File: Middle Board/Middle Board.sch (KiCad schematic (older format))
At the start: 40 parts, among them J1 JTAG Connector, SW1 SW_SPST, U1 ATSAMG55, U2 BNO055_Breakout, U3 MS5803, U4 XBee_PRO_SX

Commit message: Added GPS to mainboard schematic
Went with a different GPS module than the one Daniel picked out since
we're going with external antennas
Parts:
- added D1, D2: LED_R, symbol LED
- added D3: LED_G, symbol LED
- added D4: LED_B, symbol LED
- added J? (x2): Conn_Coaxial, symbol Conn_Coaxial
- added R1, R2, R3, R4: 270, symbol R
- added R?: 100, symbol R
- added U?: PD0922J5050S2HF, symbol PD0922J5050S2HF
- gave numbers to parts that had none: 4
- renumbered D1 to D5, D2 to D6, D3 to D7, R6 to R10, R7 to R11, R8 to R12, R9 to R14, R10 to R15, R11 to R16, R1 to R5, R2 to R6, R3 to R7, R4 to R8, R5 to R9, U4 to U5
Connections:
- net +3V3: now also D1.2 (A), D2.2 (A), D3.2 (A), D4.2 (A)
- net GND: now also J?.2 (Ext), J?.2 (Ext), R1.2
- net at U1.6 (PA0): now also R2.2
- net at U1.61 (PA2): now also R4.2
- net at U1.7 (PA1): now also R3.2
- net XBEE_RF_50Ω: now reaches U4.2, U5.36 (RF_PAD)
- net ANT1_RF_50Ω: now reaches J2.1 (In), R13.1, U4.6
- net ANT2_RF_50Ω: now reaches J3.1 (In), R13.2, U4.4
- new net: D1.1 (K), R1.1
- new net: D2.1 (K), R2.1
- new net: D3.1 (K), R3.1
- new net: D4.1 (K), R4.1
- new net ANT3_RF_50Ω: J?.1 (In), R?.1, U?.6
- new net ANT4_RF_50Ω: J?.1 (In), R?.2, U?.4
- new net GPS_RF_50Ω: U?.2
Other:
- note added: "Might need more antenna connectors, 2 might not be enough\n"
- moved on the sheet: C1, C10, C11, C12, C13, C14, C15, C16, C2, C3, C4, C5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

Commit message: Apparently I forgot to save everything earlier
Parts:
- added BT1: CR_1220, symbol Battery_Cell
- added FL1: B39162B3520U410, symbol B39162B3520U410
- added R18, R19: 20, symbol R
- added U7: UBX_NEO_M8Q, symbol UBX_NEO_M8Q
- gave numbers to parts that had none: 4
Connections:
- net +3V3: now also U7.23 (VCC)
- net GND: now also BT1.2 (-), FL1.1 (GND), FL1.3 (GND), FL1.4 (GND), FL1.6 (GND), U7.10 (GND), U7.12 (GND), U7.13 (GND), U7.24 (GND), U7.7 (VDD_USB)
- net GPS_RF_50Ω: now also FL1.5 (OUT), U7.11 (RF_IN); no longer U6.2
- new net: R18.1, U7.20 (TxD)
- new net: R19.1, U7.21 (RxD)
- new net: BT1.1 (+), U7.22 (V_BCKP)
- new net GPS_FILT_RF_50Ω: FL1.2 (IN), U6.2
- new net GPS_RX: R19.2
- new net GPS_TX: R18.2
- no-connect marks 24 -> 34
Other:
- moved on the sheet: J4, J5, R17, U6

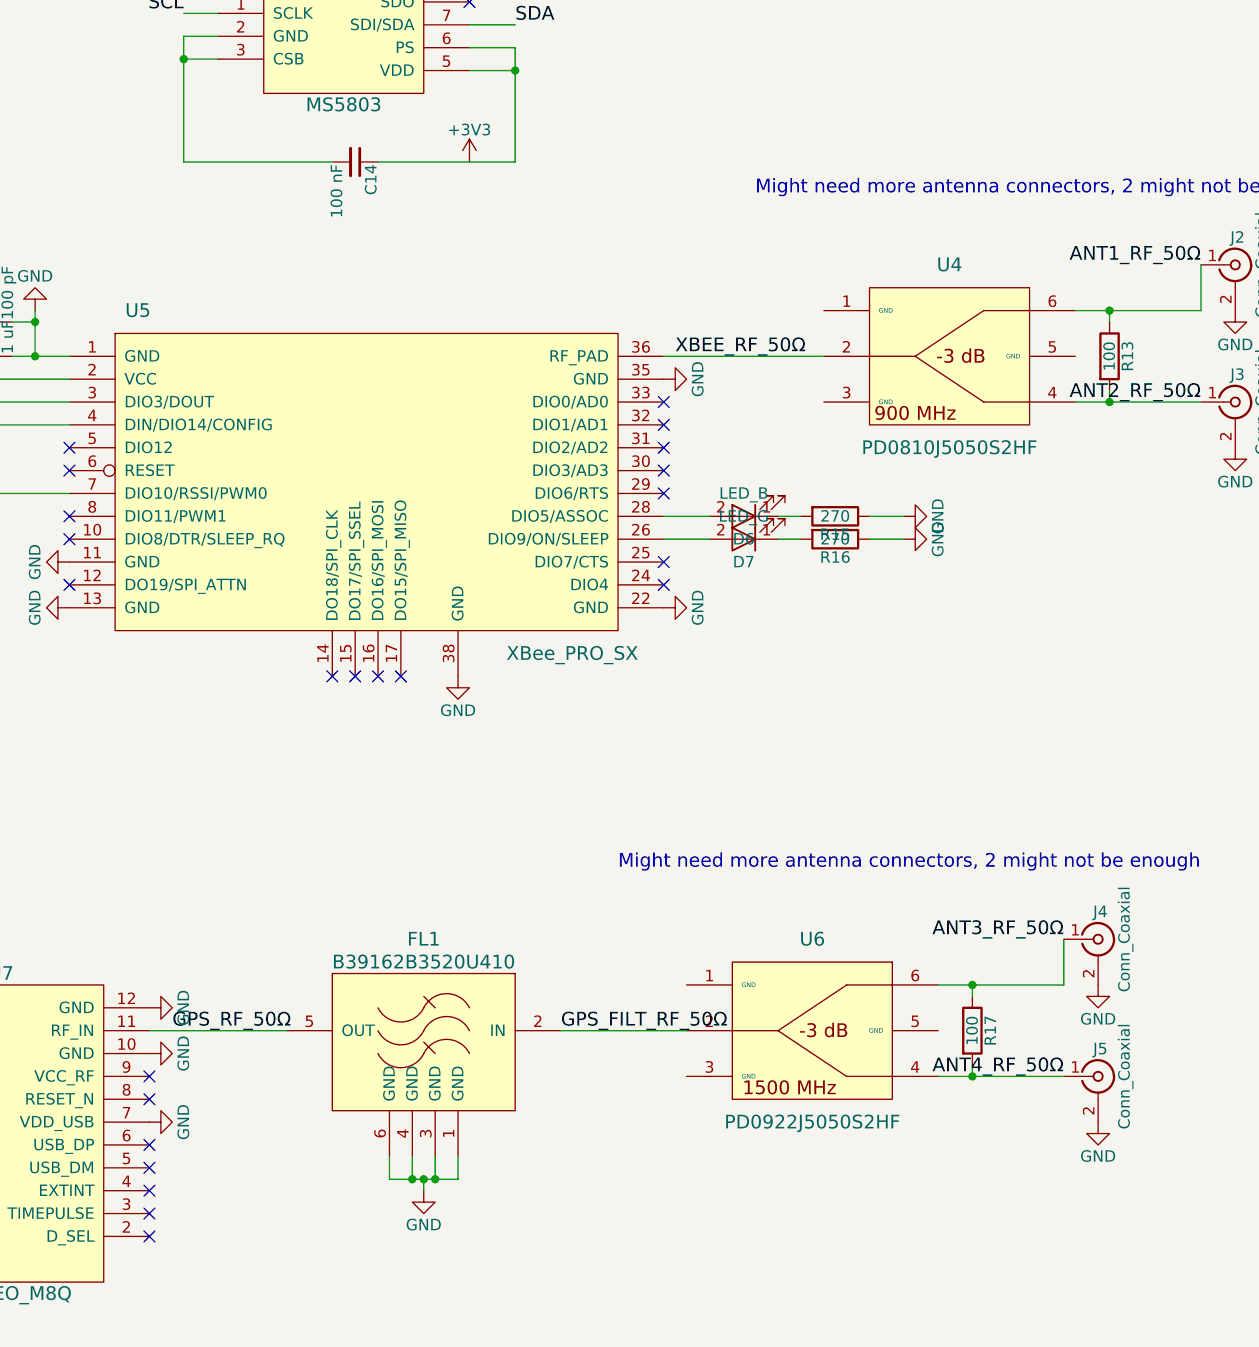
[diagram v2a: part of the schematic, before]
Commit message: Forgot ground in power dividers
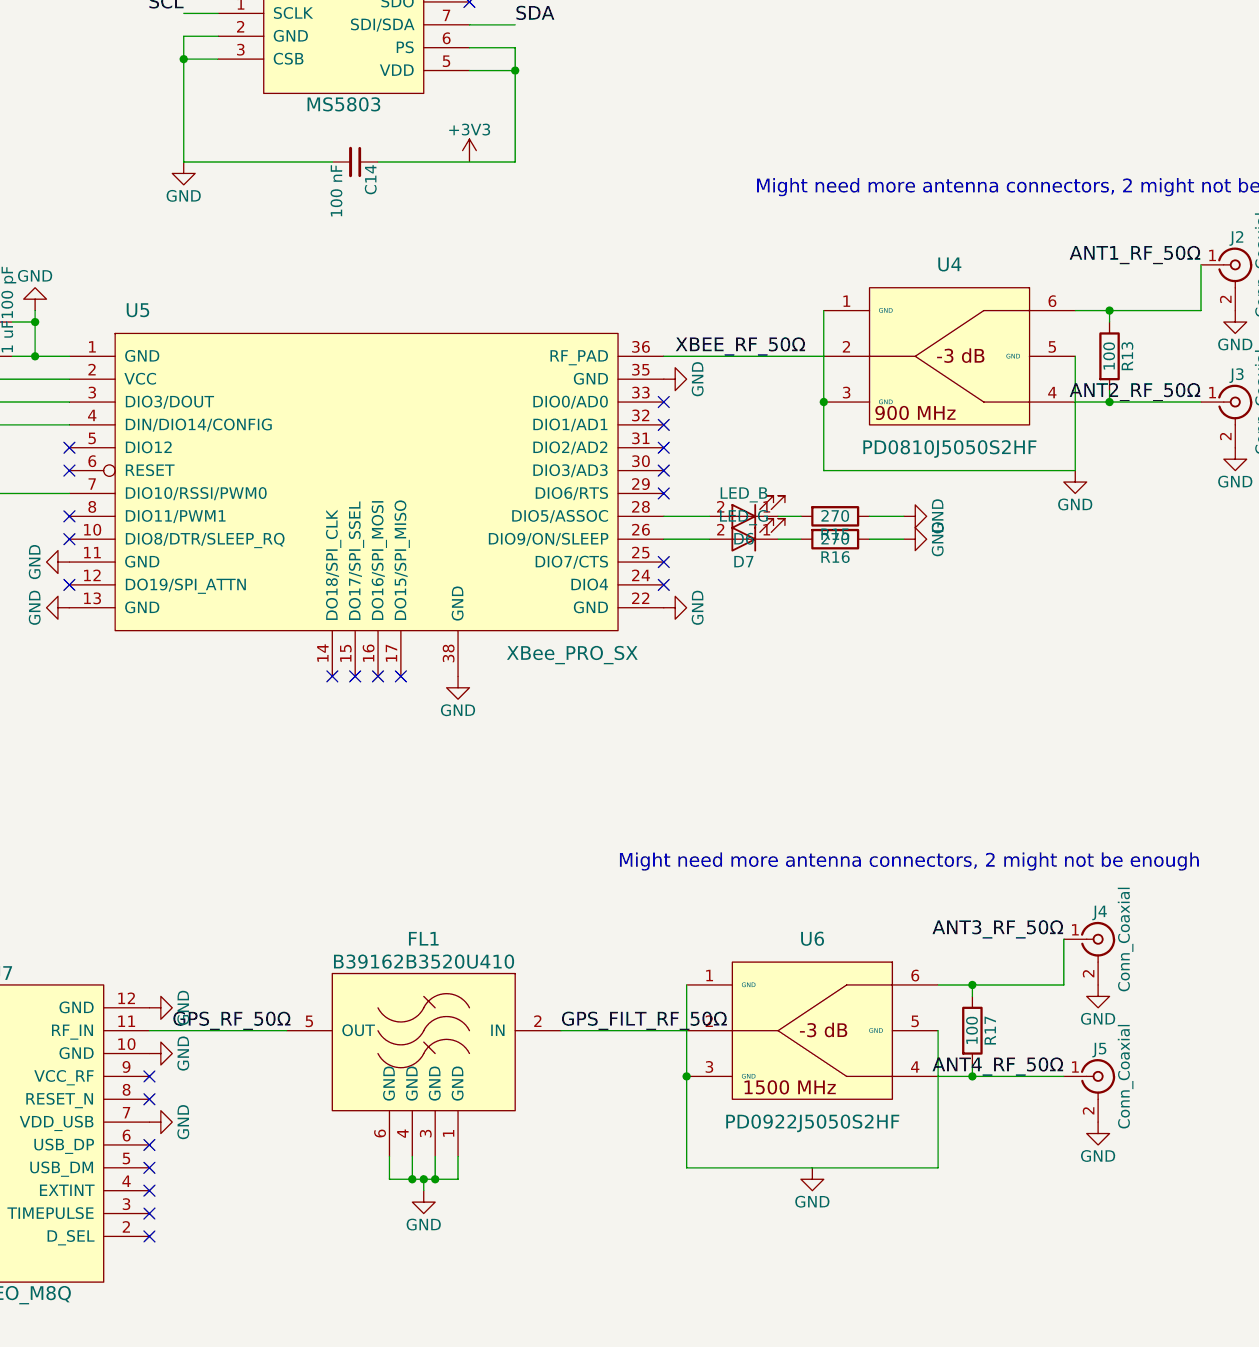
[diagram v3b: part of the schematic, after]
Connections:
- net GND: now also C14.2, U3.2 (GND), U3.3 (CSB), U4.1 (GND), U4.3 (GND), U4.5 (GND)
- net at U6.1 (GND): now also U6.3 (GND), U6.5 (GND)
